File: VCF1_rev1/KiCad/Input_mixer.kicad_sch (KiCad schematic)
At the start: 28 parts, among them J2 AudioJack2_SwitchT, J3 AudioJack2_SwitchT, J4 AudioJack2_SwitchT, Q1 Q_NPN_BCE, U1 Opamp_Quad

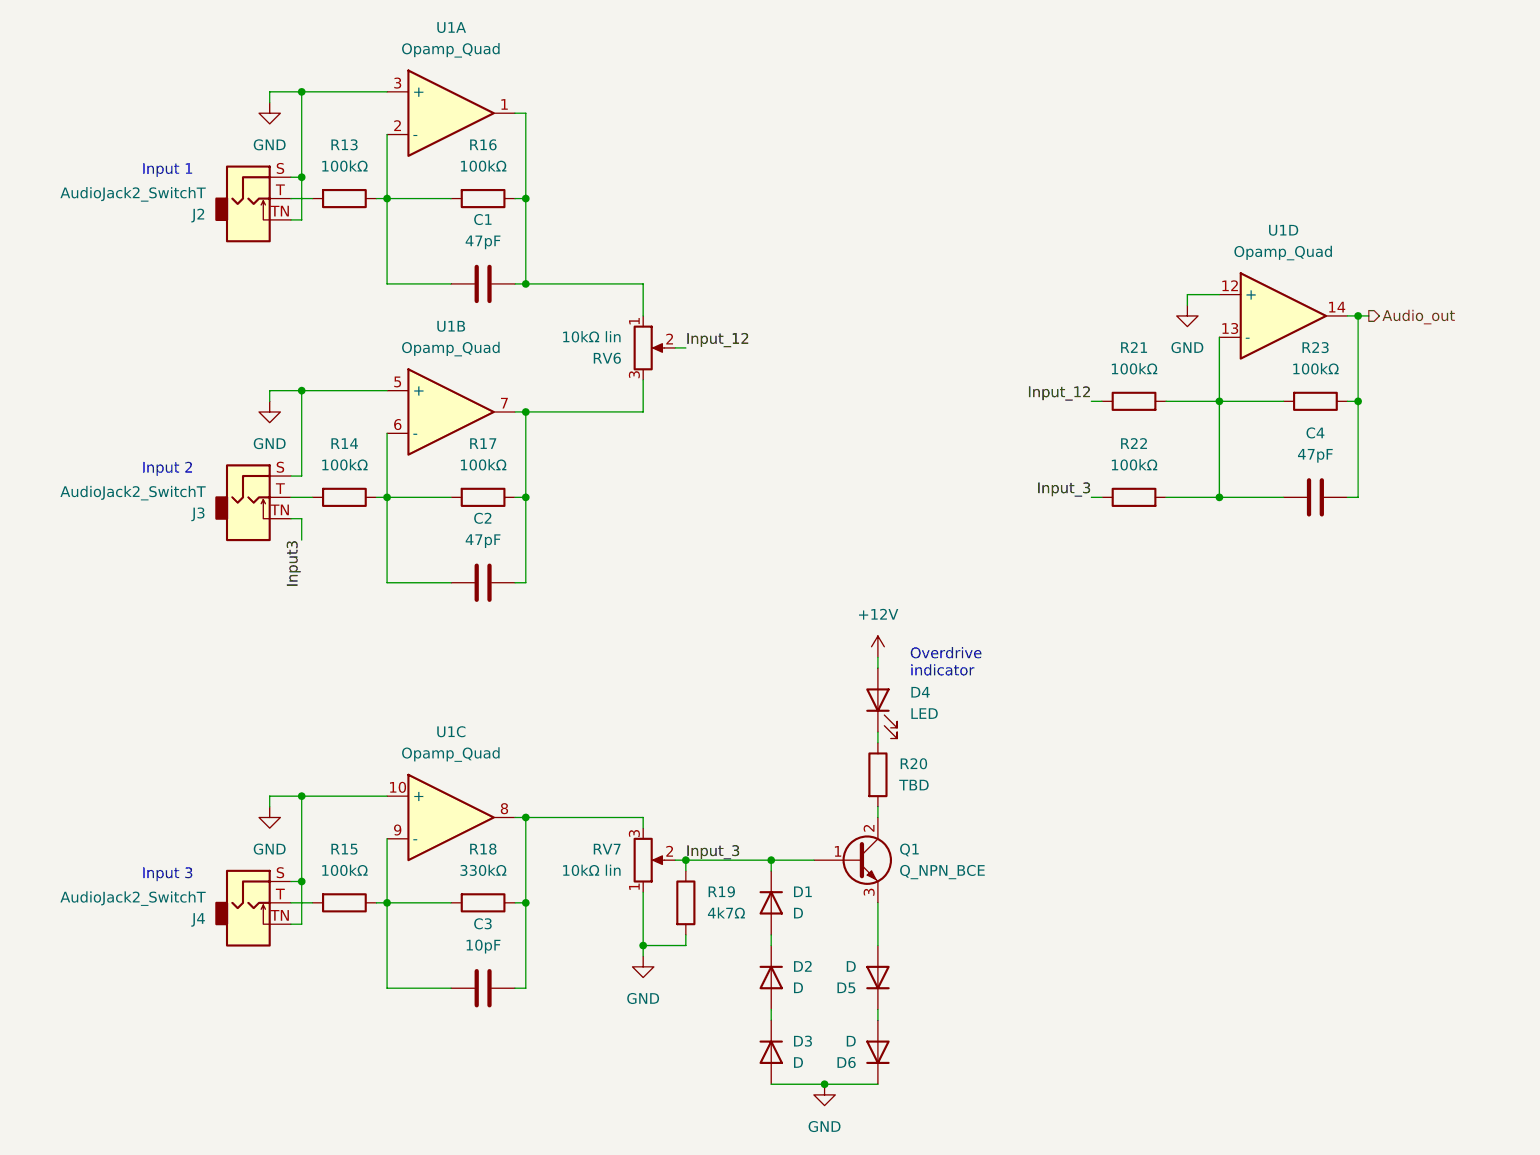
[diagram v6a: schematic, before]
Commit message: Cleaned up the first page with the overview and tried to make it a bit more readable.
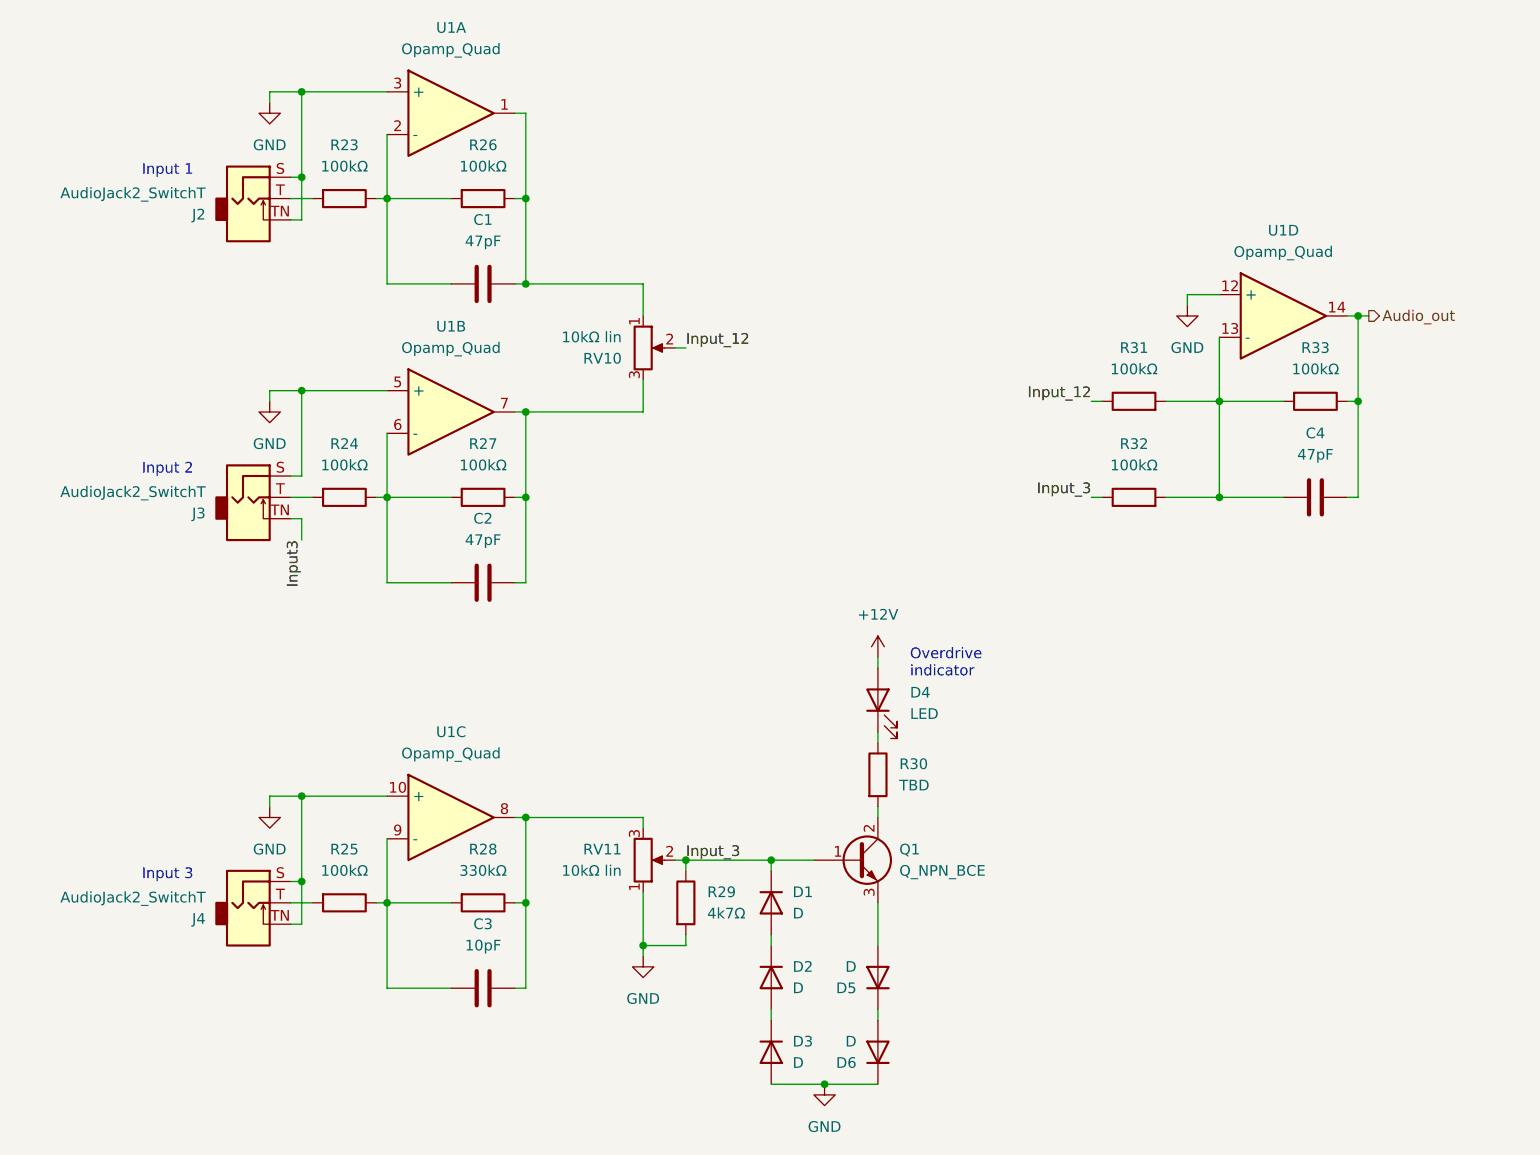
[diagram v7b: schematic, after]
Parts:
- renumbered R13 to R23, R14 to R24, R15 to R25, R16 to R26, R17 to R27, R18 to R28, R19 to R29, R20 to R30, R21 to R31, R22 to R32, R23 to R33, RV6 to RV10, RV7 to RV11

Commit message: Drew a better symbol for LM13700 because the other one was ugly.
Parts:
- R23, R24, R25, R26, R27, R28, R29, R30, R31, R32, R33: footprint (none) -> Resistor_SMD:R_0603_1608Metric
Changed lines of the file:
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@@
 (kicad_sch (version 20210621) (generator eeschema)
   (paper "A4")
+  (junction (at 90.17 133.35) (diameter 0) (color 0 0 0 0))
+  (junction (at 135.89 128.27) (diameter 0) (color 0 0 0 0))
+  (junction (at 80.01 36.83) (diameter 0) (color 0 0 0 0))
+  (junction (at 106.68 59.69) (diameter 0) (color 0 0 0 0))
+  (junction (at 120.65 138.43) (diameter 0) (color 0 0 0 0))
+  (junction (at 106.68 85.09) (diameter 0) (color 0 0 0 0))
+  (junction (at 80.01 120.65) (diameter 0) (color 0 0 0 0))
+  (junction (at 106.68 123.19) (diameter 0) (color 0 0 0 0))
+  (junction (at 189.23 73.66) (diameter 0) (color 0 0 0 0))
+  (junction (at 80.01 46.99) (diameter 0) (color 0 0 0 0))
+  (junction (at 125.73 128.27) (diameter 0) (color 0 0 0 0))
+  (junction (at 90.17 85.09) (diameter 0) (color 0 0 0 0))
+  (junction (at 205.74 63.5) (diameter 0) (color 0 0 0 0))
   (junction (at 106.68 49.53) (diameter 0) (color 0 0 0 0))
-  (junction (at 205.74 63.5) (diameter 0) (color 0 0 0 0))
-  (junction (at 90.17 85.09) (diameter 0) (color 0 0 0 0))
+  (junction (at 80.01 130.81) (diameter 0) (color 0 0 0 0))
+  (junction (at 142.24 154.94) (diameter 0) (color 0 0 0 0))
   (junction (at 106.68 74.93) (diameter 0) (color 0 0 0 0))
-  (junction (at 120.65 138.43) (diameter 0) (color 0 0 0 0))
-  (junction (at 125.73 128.27) (diameter 0) (color 0 0 0 0))
-  (junction (at 80.01 46.99) (diameter 0) (color 0 0 0 0))
+  (junction (at 106.68 133.35) (diameter 0) (color 0 0 0 0))
   (junction (at 90.17 49.53) (diameter 0) (color 0 0 0 0))
   (junction (at 80.01 72.39) (diameter 0) (color 0 0 0 0))
-  (junction (at 106.68 85.09) (diameter 0) (color 0 0 0 0))
-  (junction (at 80.01 36.83) (diameter 0) (color 0 0 0 0))
-  (junction (at 80.01 120.65) (diameter 0) (color 0 0 0 0))
-  (junction (at 106.68 133.35) (diameter 0) (color 0 0 0 0))
+  (junction (at 205.74 73.66) (diameter 0) (color 0 0 0 0))
   (junction (at 189.23 85.09) (diameter 0) (color 0 0 0 0))
-  (junction (at 142.24 154.94) (diameter 0) (color 0 0 0 0))
-  (junction (at 80.01 130.81) (diameter 0) (color 0 0 0 0))
-  (junction (at 135.89 128.27) (diameter 0) (color 0 0 0 0))
-  (junction (at 106.68 123.19) (diameter 0) (color 0 0 0 0))
-  (junction (at 205.74 73.66) (diameter 0) (color 0 0 0 0))
-  (junction (at 189.23 73.66) (diameter 0) (color 0 0 0 0))
-  (junction (at 90.17 133.35) (diameter 0) (color 0 0 0 0))
-  (junction (at 106.68 59.69) (diameter 0) (color 0 0 0 0))
   (wire (pts (xy 106.68 39.37) (xy 105.41 39.37))
     (stroke (width 0) (type default) (color 0 0 0 0))
@@
     (stroke (width 0) (type default) (color 0 0 0 0))
   )
+  (wire (pts (xy 124.46 128.27) (xy 125.73 128.27))
+    (stroke (width 0) (type default) (color 0 0 0 0))
+  )
+  (wire (pts (xy 125.73 128.27) (xy 135.89 128.27))
+    (stroke (width 0) (type default) (color 0 0 0 0))
+  )
   (wire (pts (xy 135.89 128.27) (xy 140.97 128.27))
     (stroke (width 0) (type default) (color 0 0 0 0))
   )
-  (wire (pts (xy 125.73 128.27) (xy 135.89 128.27))
-    (stroke (width 0) (type default) (color 0 0 0 0))
-  )
-  (wire (pts (xy 124.46 128.27) (xy 125.73 128.27))
-    (stroke (width 0) (type default) (color 0 0 0 0))
-  )
   (wire (pts (xy 106.68 59.69) (xy 106.68 49.53))
     (stroke (width 0) (type default) (color 0 0 0 0))
@@
     (stroke (width 0) (type default) (color 0 0 0 0))
   )
+  (wire (pts (xy 120.65 132.08) (xy 120.65 138.43))
+    (stroke (width 0) (type default) (color 0 0 0 0))
+  )
   (wire (pts (xy 120.65 138.43) (xy 120.65 139.7))
     (stroke (width 0) (type default) (color 0 0 0 0))
   )
-  (wire (pts (xy 120.65 132.08) (xy 120.65 138.43))
-    (stroke (width 0) (type default) (color 0 0 0 0))
-  )
   (wire (pts (xy 135.89 128.27) (xy 135.89 129.54))
     (stroke (width 0) (type default) (color 0 0 0 0))
@@
     (stroke (width 0) (type default) (color 0 0 0 0))
   )
+  (wire (pts (xy 78.74 46.99) (xy 80.01 46.99))
+    (stroke (width 0) (type default) (color 0 0 0 0))
+  )
   (wire (pts (xy 80.01 46.99) (xy 80.01 52.07))
-    (stroke (width 0) (type default) (color 0 0 0 0))
-  )
-  (wire (pts (xy 78.74 46.99) (xy 80.01 46.99))
     (stroke (width 0) (type default) (color 0 0 0 0))
   )
@@
       (effects (font (size 1.27 1.27)) (justify left))
     )
-    (property "Footprint" "" (id 2) (at 123.952 133.35 90)
+    (property "Footprint" "Resistor_SMD:R_0603_1608Metric" (id 2) (at 123.952 133.35 90)
       (effects (font (size 1.27 1.27)) hide)
     )
@@
       (effects (font (size 1.27 1.27)) (justify left))
     )
-    (property "Footprint" "" (id 2) (at 146.812 118.11 90)
+    (property "Footprint" "Resistor_SMD:R_0603_1608Metric" (id 2) (at 146.812 118.11 90)
       (effects (font (size 1.27 1.27)) hide)
     )
@@
     (property "Reference" "R24" (id 0) (at 85.09 78.74 90))
     (property "Value" "100kΩ" (id 1) (at 85.09 81.28 90))
-    (property "Footprint" "" (id 2) (at 85.09 83.312 90)
+    (property "Footprint" "Resistor_SMD:R_0603_1608Metric" (id 2) (at 85.09 83.312 90)
       (effects (font (size 1.27 1.27)) hide)
     )
@@
     (property "Reference" "R26" (id 0) (at 101.6 43.18 90))
     (property "Value" "100kΩ" (id 1) (at 101.6 45.72 90))
-    (property "Footprint" "" (id 2) (at 101.6 47.752 90)
+    (property "Footprint" "Resistor_SMD:R_0603_1608Metric" (id 2) (at 101.6 47.752 90)
       (effects (font (size 1.27 1.27)) hide)
     )
@@
     (property "Reference" "R25" (id 0) (at 85.09 127 90))
     (property "Value" "100kΩ" (id 1) (at 85.09 129.54 90))
-    (property "Footprint" "" (id 2) (at 85.09 131.572 90)
+    (property "Footprint" "Resistor_SMD:R_0603_1608Metric" (id 2) (at 85.09 131.572 90)
       (effects (font (size 1.27 1.27)) hide)
     )
@@
     (property "Reference" "R28" (id 0) (at 101.6 127 90))
     (property "Value" "330kΩ" (id 1) (at 101.6 129.54 90))
-    (property "Footprint" "" (id 2) (at 101.6 131.572 90)
+    (property "Footprint" "Resistor_SMD:R_0603_1608Metric" (id 2) (at 101.6 131.572 90)
       (effects (font (size 1.27 1.27)) hide)
     )
@@
     (property "Reference" "R32" (id 0) (at 179.07 78.74 90))
     (property "Value" "100kΩ" (id 1) (at 179.07 81.28 90))
-    (property "Footprint" "" (id 2) (at 179.07 86.868 90)
+    (property "Footprint" "Resistor_SMD:R_0603_1608Metric" (id 2) (at 179.07 86.868 90)
       (effects (font (size 1.27 1.27)) hide)
     )
@@
     (property "Reference" "R23" (id 0) (at 85.09 43.18 90))
     (property "Value" "100kΩ" (id 1) (at 85.09 45.72 90))
-    (property "Footprint" "" (id 2) (at 85.09 47.752 90)
+    (property "Footprint" "Resistor_SMD:R_0603_1608Metric" (id 2) (at 85.09 47.752 90)
       (effects (font (size 1.27 1.27)) hide)
     )
@@
     (property "Reference" "R27" (id 0) (at 101.6 78.74 90))
     (property "Value" "100kΩ" (id 1) (at 101.6 81.28 90))
-    (property "Footprint" "" (id 2) (at 101.6 83.312 90)
+    (property "Footprint" "Resistor_SMD:R_0603_1608Metric" (id 2) (at 101.6 83.312 90)
       (effects (font (size 1.27 1.27)) hide)
     )
@@
     (property "Reference" "R31" (id 0) (at 179.07 67.31 90))
     (property "Value" "100kΩ" (id 1) (at 179.07 69.85 90))
-    (property "Footprint" "" (id 2) (at 179.07 75.438 90)
+    (property "Footprint" "Resistor_SMD:R_0603_1608Metric" (id 2) (at 179.07 75.438 90)
       (effects (font (size 1.27 1.27)) hide)
     )
@@
     (property "Reference" "R33" (id 0) (at 200.66 67.31 90))
     (property "Value" "100kΩ" (id 1) (at 200.66 69.85 90))
-    (property "Footprint" "" (id 2) (at 200.66 71.882 90)
-      (effects (font (size 1.27 1.27)) hide)
-    )
+    (property "Footprint" "Resistor_SMD:R_0603_1608Metric" (id 2) (at 200.66 71.882 90)
+      (effects (font (size 1.27 1.27)) hide)
+    )
